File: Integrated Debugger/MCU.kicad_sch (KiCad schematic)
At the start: 14 parts, among them SW2 BOOT, U3 STM32F103CBUx, Y1 8MHz

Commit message: feat: finish routing of components
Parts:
- SW2: footprint Picoballoon Mechanical & Misc:Button GT-TC029B-H025-L1N -> Picoballoon Mechanical & Misc:Button SMD-4P,2.5x1.6mm
- Y1: footprint (none) -> Picoballoon Passives:Crystal CSTNE8M00GH5C000R0
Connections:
- net GND: now also C3.1, U3.44 (BOOT0), Y1.2
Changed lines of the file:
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@@
 	)
 	(junction
+		(at 107.95 35.56)
+		(diameter 0)
+		(color 0 0 0 0)
+	)
+	(junction
 		(at 181.61 57.15)
 		(diameter 0)
@@
 	(wire
 		(pts
+			(xy 107.95 35.56) (xy 107.95 39.37)
+		)
+		(stroke
+			(width 0)
+			(type default)
+		)
+	)
+	(wire
+		(pts
 			(xy 88.9 20.32) (xy 88.9 30.48)
 		)
@@
 	(wire
 		(pts
-			(xy 88.9 35.56) (xy 115.57 35.56)
+			(xy 88.9 35.56) (xy 107.95 35.56)
 		)
 		(stroke
@@
 	(wire
 		(pts
+			(xy 107.95 35.56) (xy 115.57 35.56)
+		)
+		(stroke
+			(width 0)
+			(type default)
+		)
+	)
+	(wire
+		(pts
 			(xy 115.57 54.61) (xy 115.57 58.42)
 		)
@@
 		)
 		(instances
-			(project ""
+			(project "Integrated Debugger"
 				(path "/ce538ebe-fda9-4af3-9f8c-9fd5bf58f0e4/b916d44a-03d1-4a04-a023-19b38caca2ea"
 					(reference "U3")
@@
 		)
 		(instances
-			(project "Programmer"
+			(project "Integrated Debugger"
 				(path "/ce538ebe-fda9-4af3-9f8c-9fd5bf58f0e4/b916d44a-03d1-4a04-a023-19b38caca2ea"
 					(reference "C7")
@@
 		)
 		(instances
-			(project "Programmer"
+			(project "Integrated Debugger"
 				(path "/ce538ebe-fda9-4af3-9f8c-9fd5bf58f0e4/b916d44a-03d1-4a04-a023-19b38caca2ea"
 					(reference "C3")
@@
 			)
 		)
-		(property "Footprint" "Picoballoon Mechanical & Misc:Button GT-TC029B-H025-L1N"
+		(property "Footprint" "Picoballoon Mechanical & Misc:Button SMD-4P,2.5x1.6mm"
 			(at 93.98 99.06 0)
 			(effects
@@
 		)
 		(instances
-			(project ""
+			(project "Integrated Debugger"
 				(path "/ce538ebe-fda9-4af3-9f8c-9fd5bf58f0e4/b916d44a-03d1-4a04-a023-19b38caca2ea"
 					(reference "SW2")
@@
 		)
 		(instances
-			(project ""
+			(project "Integrated Debugger"
 				(path "/ce538ebe-fda9-4af3-9f8c-9fd5bf58f0e4/b916d44a-03d1-4a04-a023-19b38caca2ea"
 					(reference "C4")
@@
 		)
 		(instances
-			(project "Programmer"
+			(project "Integrated Debugger"
 				(path "/ce538ebe-fda9-4af3-9f8c-9fd5bf58f0e4/b916d44a-03d1-4a04-a023-19b38caca2ea"
 					(reference "C8")
@@
 		)
 		(instances
-			(project "Programmer"
+			(project "Integrated Debugger"
 				(path "/ce538ebe-fda9-4af3-9f8c-9fd5bf58f0e4/b916d44a-03d1-4a04-a023-19b38caca2ea"
 					(reference "R14")
@@
 		)
 		(instances
-			(project "Programmer"
+			(project "Integrated Debugger"
 				(path "/ce538ebe-fda9-4af3-9f8c-9fd5bf58f0e4/b916d44a-03d1-4a04-a023-19b38caca2ea"
 					(reference "C5")
@@
 		)
 		(instances
-			(project "Programmer"
+			(project "Integrated Debugger"
 				(path "/ce538ebe-fda9-4af3-9f8c-9fd5bf58f0e4/b916d44a-03d1-4a04-a023-19b38caca2ea"
 					(reference "C6")
@@
 	(symbol
 		(lib_id "Picoballoon Power Symbols:GND")
+		(at 107.95 39.37 0)
+		(unit 1)
+		(exclude_from_sim no)
+		(in_bom yes)
+		(on_board yes)
+		(dnp no)
+		(fields_autoplaced yes)
+		(property "Reference" "#PWR019"
+			(at 107.95 45.72 0)
+			(effects
+				(font
+					(size 1.27 1.27)
+				)
+				(hide yes)
+			)
+		)
+		(property "Value" "GND"
+			(at 107.95 43.18 0)
+			(do_not_autoplace yes)
+			(effects
+				(font
+					(size 1.27 1.27)
+				)
+			)
+		)
+		(property "Footprint" ""
+			(at 107.95 39.37 0)
+			(effects
+				(font
+					(size 1.27 1.27)
+				)
+				(hide yes)
+			)
+		)
+		(property "Datasheet" ""
+			(at 107.95 39.37 0)
+			(effects
+				(font
+					(size 1.27 1.27)
+				)
+				(hide yes)
+			)
+		)
+		(property "Description" "Power symbol creates a global label with name \"GND\" , ground"
+			(at 107.95 39.37 0)
+			(effects
+				(font
+					(size 1.27 1.27)
+				)
+				(hide yes)
+			)
+		)
+		(pin "1"
+		)
+		(instances
+			(project "Integrated Debugger"
+				(path "/ce538ebe-fda9-4af3-9f8c-9fd5bf58f0e4/b916d44a-03d1-4a04-a023-19b38caca2ea"
+					(reference "#PWR019")
+					(unit 1)
+				)
+			)
+		)
+	)
+	(symbol
+		(lib_id "Picoballoon Power Symbols:GND")
 		(at 58.42 111.76 0)
 		(unit 1)
@@
 		)
 		(instances
-			(project ""
+			(project "Integrated Debugger"
 				(path "/ce538ebe-fda9-4af3-9f8c-9fd5bf58f0e4/b916d44a-03d1-4a04-a023-19b38caca2ea"
 					(reference "#PWR010")
@@
 		)
 		(instances
-			(project "Programmer"
+			(project "Integrated Debugger"
 				(path "/ce538ebe-fda9-4af3-9f8c-9fd5bf58f0e4/b916d44a-03d1-4a04-a023-19b38caca2ea"
 					(reference "R19")
@@
 		)
 		(instances
-			(project ""
+			(project "Integrated Debugger"
 				(path "/ce538ebe-fda9-4af3-9f8c-9fd5bf58f0e4/b916d44a-03d1-4a04-a023-19b38caca2ea"
 					(reference "#PWR012")
@@
 		)
 		(instances
-			(project "Programmer"
+			(project "Integrated Debugger"
 				(path "/ce538ebe-fda9-4af3-9f8c-9fd5bf58f0e4/b916d44a-03d1-4a04-a023-19b38caca2ea"
 					(reference "R15")
@@
 		)
 		(instances
-			(project "Programmer"
+			(project "Integrated Debugger"
 				(path "/ce538ebe-fda9-4af3-9f8c-9fd5bf58f0e4/b916d44a-03d1-4a04-a023-19b38caca2ea"
 					(reference "#PWR011")
@@
 		)
 		(instances
-			(project "Programmer"
+			(project "Integrated Debugger"
 				(path "/ce538ebe-fda9-4af3-9f8c-9fd5bf58f0e4/b916d44a-03d1-4a04-a023-19b38caca2ea"
 					(reference "#PWR013")
@@
 		)
 		(instances
-			(project "Programmer"
+			(project "Integrated Debugger"
 				(path "/ce538ebe-fda9-4af3-9f8c-9fd5bf58f0e4/b916d44a-03d1-4a04-a023-19b38caca2ea"
 					(reference "#PWR015")
@@
 		)
 		(instances
-			(project "Programmer"
+			(project "Integrated Debugger"
 				(path "/ce538ebe-fda9-4af3-9f8c-9fd5bf58f0e4/b916d44a-03d1-4a04-a023-19b38caca2ea"
 					(reference "C9")
@@
 		)
 		(instances
-			(project "Programmer"
+			(project "Integrated Debugger"
 				(path "/ce538ebe-fda9-4af3-9f8c-9fd5bf58f0e4/b916d44a-03d1-4a04-a023-19b38caca2ea"
 					(reference "#PWR014")
@@
 			)
 		)
-		(property "Footprint" ""
+		(property "Footprint" "Picoballoon Passives:Crystal CSTNE8M00GH5C000R0"
 			(at 78.105 40.64 0)
 			(effects
@@
 		)
 		(instances
-			(project ""
+			(project "Integrated Debugger"
 				(path "/ce538ebe-fda9-4af3-9f8c-9fd5bf58f0e4/b916d44a-03d1-4a04-a023-19b38caca2ea"
 					(reference "Y1")
@@
 		)
 		(instances
-			(project "Programmer"
+			(project "Integrated Debugger"
 				(path "/ce538ebe-fda9-4af3-9f8c-9fd5bf58f0e4/b916d44a-03d1-4a04-a023-19b38caca2ea"
 					(reference "R13")

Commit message: feat: add manufacturing data
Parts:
- C3, C4, C5, C6, C7: JLCPCB Part # (none) -> C76934; LCSC Part # (none) -> C76934; MPN (none) -> GRM033R61A104KE15D
- C8: JLCPCB Part # (none) -> C76930; LCSC Part # (none) -> C76930; MPN (none) -> GRM033R60J105MEA2D
- C9: JLCPCB Part # (none) -> C335103; LCSC Part # (none) -> C335103; MPN (none) -> GRM035R60J475ME15D
- R13, R15: JLCPCB Part # (none) -> C717002; LCSC Part # (none) -> C717002; MPN (none) -> ERJ1GNF1002C
- R14: JLCPCB Part # (none) -> C138135; LCSC Part # (none) -> C138135; MPN (none) -> RC0201FR-074K7L
- R19: JLCPCB Part # (none) -> C106227; LCSC Part # (none) -> C106227; MPN (none) -> RC0201FR-070RL
- SW2: LCSC Part # (none) -> C25168822; MPN (none) -> HX TS152605A 160gf
- U3: JLCPCB Part # (none) -> C55506; LCSC Part # (none) -> C55506; MPN (none) -> STM32F103CBU6
- Y1: JLCPCB Part # (none) -> C341525; LCSC Part # (none) -> C341525; MPN (none) -> CSTNE8M00GH5C000R0

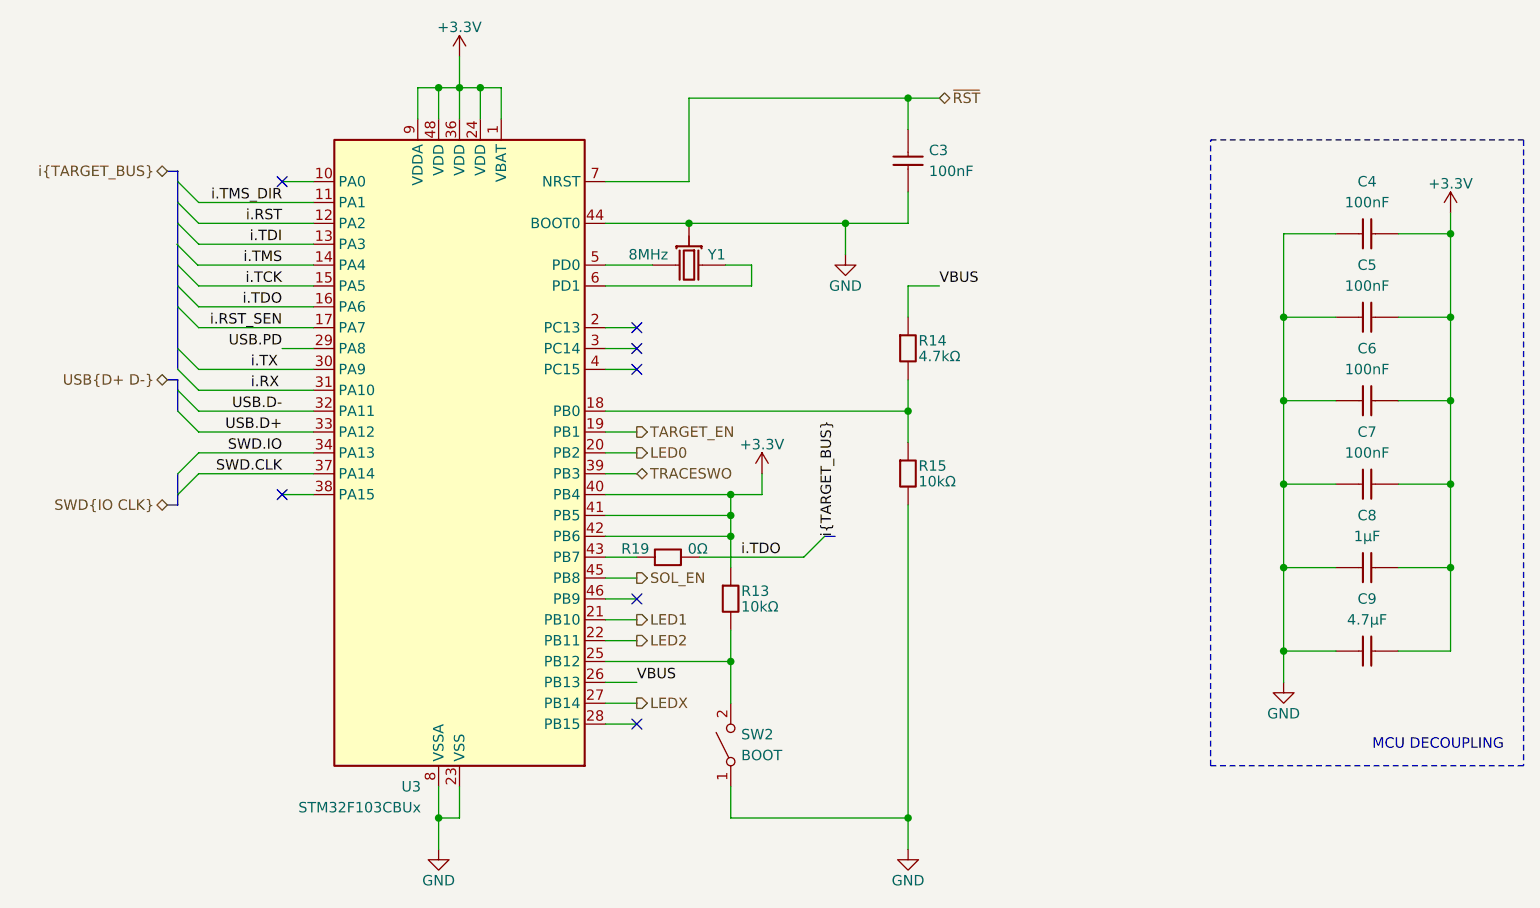
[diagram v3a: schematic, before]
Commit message: Schematic consistency improvements
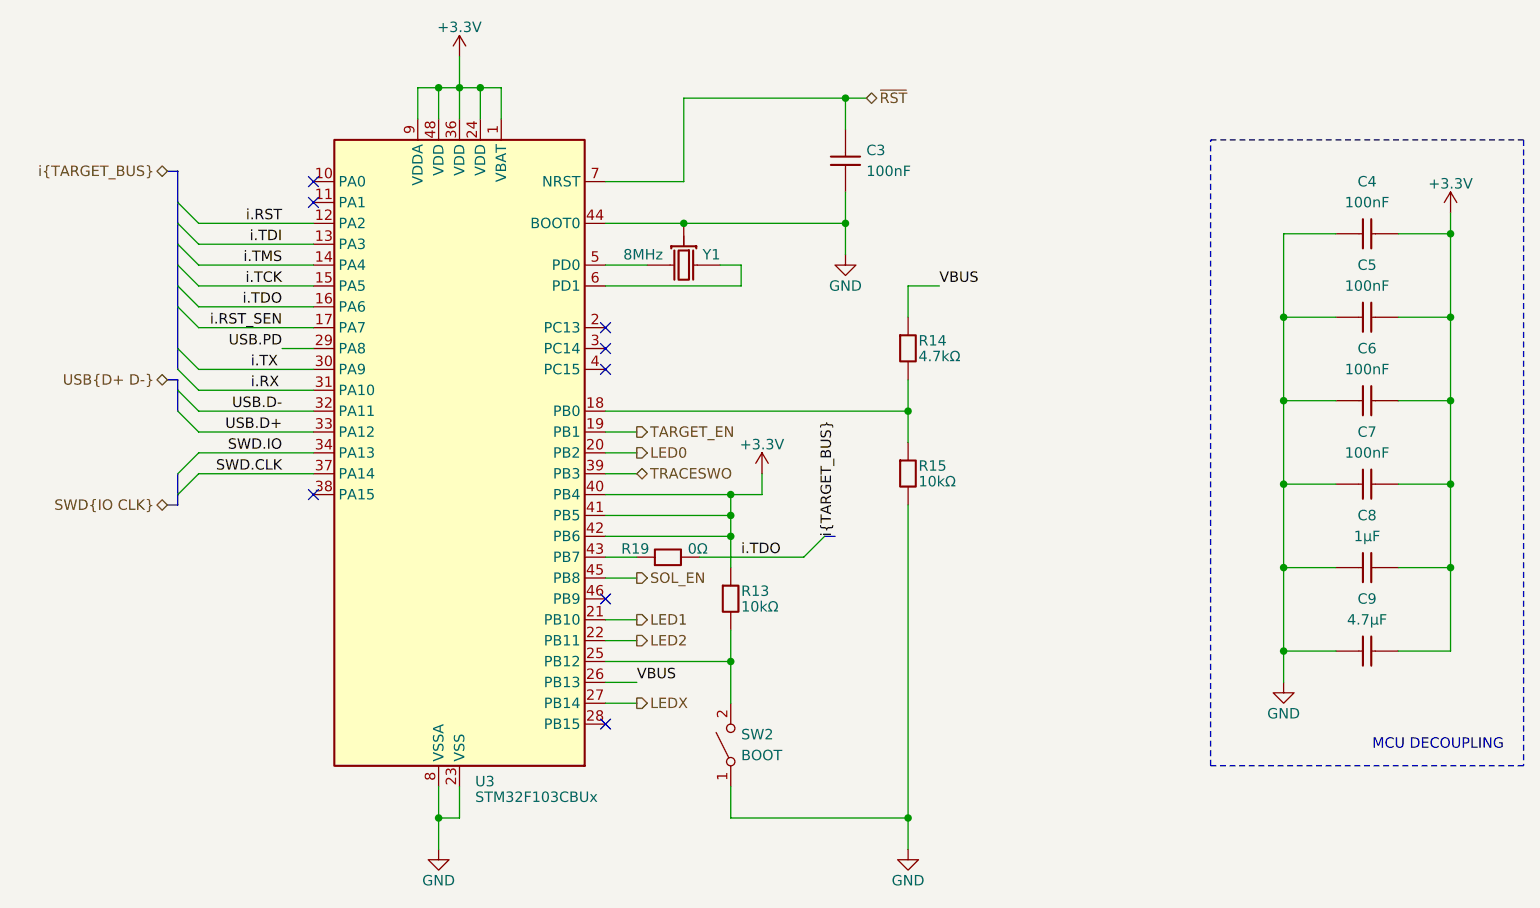
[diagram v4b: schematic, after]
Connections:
- net i.TMS_DIR: no longer names the net of U3.11 (PA1)
- no-connect marks 7 -> 8
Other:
- moved on the sheet: C3, Y1

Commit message: PCB improvements
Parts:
- renumbered C3 to C1, C4 to C2, C5 to C3, C6 to C4, C7 to C5, C8 to C6, C9 to C7, R14 to R10, R15 to R11, R19 to R8, R13 to R9, SW2 to SW1, U3 to U2
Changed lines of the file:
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@@
 	(wire
 		(pts
-			(xy 119.38 43.18) (xy 115.57 43.18)
+			(xy 121.92 43.18) (xy 115.57 43.18)
 		)
 		(stroke
@@
 	(wire
 		(pts
-			(xy 82.55 91.44) (xy 78.74 91.44)
-		)
-		(stroke
-			(width 0)
-			(type default)
-		)
-	)
-	(wire
-		(pts
 			(xy 29.21 58.42) (xy 43.18 58.42)
 		)
@@
 		)
 	)
+	(wire
+		(pts
+			(xy 78.74 91.44) (xy 88.9 91.44)
+		)
+		(stroke
+			(width 0)
+			(type default)
+		)
+	)
 	(bus
 		(pts
@@
 	)
 	(label "VBUS"
-		(at 82.55 91.44 0)
+		(at 88.9 91.44 180)
 		(effects
 			(font
 				(size 1.27 1.27)
 			)
-			(justify left bottom)
+			(justify right bottom)
 		)
 	)
@@
 	)
 	(label "VBUS"
-		(at 119.38 43.18 0)
+		(at 121.92 43.18 180)
 		(effects
 			(font
 				(size 1.27 1.27)
 			)
-			(justify left bottom)
+			(justify right bottom)
 		)
 	)
@@
 		(on_board yes)
 		(dnp no)
-		(property "Reference" "U3"
+		(property "Reference" "U2"
 			(at 62.865 103.505 0)
 			(effects
@@
 			(project "Integrated Debugger"
 				(path "/ce538ebe-fda9-4af3-9f8c-9fd5bf58f0e4/b916d44a-03d1-4a04-a023-19b38caca2ea"
-					(reference "U3")
+					(reference "U2")
 					(unit 1)
 				)
@@
 		(dnp no)
 		(fields_autoplaced yes)
-		(property "Reference" "C7"
+		(property "Reference" "C5"
 			(at 171.45 60.96 90)
 			(effects
@@
 			(project "Integrated Debugger"
 				(path "/ce538ebe-fda9-4af3-9f8c-9fd5bf58f0e4/b916d44a-03d1-4a04-a023-19b38caca2ea"
-					(reference "C7")
+					(reference "C5")
 					(unit 1)
 				)
@@
 		(dnp no)
 		(fields_autoplaced yes)
-		(property "Reference" "C3"
+		(property "Reference" "C1"
 			(at 110.49 26.6699 0)
 			(effects
@@
 			(project "Integrated Debugger"
 				(path "/ce538ebe-fda9-4af3-9f8c-9fd5bf58f0e4/b916d44a-03d1-4a04-a023-19b38caca2ea"
-					(reference "C3")
+					(reference "C1")
 					(unit 1)
 				)
@@
 		(dnp no)
 		(fields_autoplaced yes)
-		(property "Reference" "SW2"
+		(property "Reference" "SW1"
 			(at 95.25 97.7899 90)
 			(effects
@@
 			(project "Integrated Debugger"
 				(path "/ce538ebe-fda9-4af3-9f8c-9fd5bf58f0e4/b916d44a-03d1-4a04-a023-19b38caca2ea"
-					(reference "SW2")
+					(reference "SW1")
 					(unit 1)
 				)
@@
 		(dnp no)
 		(fields_autoplaced yes)
-		(property "Reference" "C4"
+		(property "Reference" "C2"
 			(at 171.45 30.48 90)
 			(effects
@@
 			(project "Integrated Debugger"
 				(path "/ce538ebe-fda9-4af3-9f8c-9fd5bf58f0e4/b916d44a-03d1-4a04-a023-19b38caca2ea"
-					(reference "C4")
+					(reference "C2")
 					(unit 1)
 				)
@@
 		(dnp no)
 		(fields_autoplaced yes)
-		(property "Reference" "C8"
+		(property "Reference" "C6"
 			(at 171.45 71.12 90)
 			(effects
@@
 			(project "Integrated Debugger"
 				(path "/ce538ebe-fda9-4af3-9f8c-9fd5bf58f0e4/b916d44a-03d1-4a04-a023-19b38caca2ea"
-					(reference "C8")
+					(reference "C6")
 					(unit 1)
 				)
@@
 		(dnp no)
 		(fields_autoplaced yes)
-		(property "Reference" "R14"
+		(property "Reference" "R10"
 			(at 116.84 49.8475 0)
 			(do_not_autoplace yes)
@@
 			(project "Integrated Debugger"
 				(path "/ce538ebe-fda9-4af3-9f8c-9fd5bf58f0e4/b916d44a-03d1-4a04-a023-19b38caca2ea"
-					(reference "R14")
+					(reference "R10")
 					(unit 1)
 				)
@@
 		(dnp no)
 		(fields_autoplaced yes)
-		(property "Reference" "C5"
+		(property "Reference" "C3"
 			(at 171.45 40.64 90)
 			(effects
@@
 			(project "Integrated Debugger"
 				(path "/ce538ebe-fda9-4af3-9f8c-9fd5bf58f0e4/b916d44a-03d1-4a04-a023-19b38caca2ea"
-					(reference "C5")
+					(reference "C3")
 					(unit 1)
 				)
@@
 		(dnp no)
 		(fields_autoplaced yes)
-		(property "Reference" "C6"
+		(property "Reference" "C4"
 			(at 171.45 50.8 90)
 			(effects
@@
 			(project "Integrated Debugger"
 				(path "/ce538ebe-fda9-4af3-9f8c-9fd5bf58f0e4/b916d44a-03d1-4a04-a023-19b38caca2ea"
-					(reference "C6")
+					(reference "C4")
 					(unit 1)
 				)
@@
 		(dnp no)
 		(fields_autoplaced yes)
-		(property "Reference" "#PWR019"
+		(property "Reference" "#PWR010"
 			(at 107.95 45.72 0)
 			(effects
@@
 			(project "Integrated Debugger"
 				(path "/ce538ebe-fda9-4af3-9f8c-9fd5bf58f0e4/b916d44a-03d1-4a04-a023-19b38caca2ea"
-					(reference "#PWR019")
+					(reference "#PWR010")
 					(unit 1)
 				)
@@
 		(dnp no)
 		(fields_autoplaced yes)
-		(property "Reference" "#PWR010"
+		(property "Reference" "#PWR07"
 			(at 58.42 118.11 0)
 			(effects
@@
 			(project "Integrated Debugger"
 				(path "/ce538ebe-fda9-4af3-9f8c-9fd5bf58f0e4/b916d44a-03d1-4a04-a023-19b38caca2ea"
-					(reference "#PWR010")
+					(reference "#PWR07")
 					(unit 1)
 				)
@@
 		(on_board yes)
 		(dnp no)
-		(property "Reference" "R19"
+		(property "Reference" "R8"
 			(at 84.074 75.184 90)
 			(do_not_autoplace yes)
@@
 			(project "Integrated Debugger"
 				(path "/ce538ebe-fda9-4af3-9f8c-9fd5bf58f0e4/b916d44a-03d1-4a04-a023-19b38caca2ea"
-					(reference "R19")
+					(reference "R8")
 					(unit 1)
 				)
@@
 		(dnp no)
 		(fields_autoplaced yes)
-		(property "Reference" "#PWR012"
+		(property "Reference" "#PWR09"
 			(at 97.79 69.85 0)
 			(effects
@@
 			(project "Integrated Debugger"
 				(path "/ce538ebe-fda9-4af3-9f8c-9fd5bf58f0e4/b916d44a-03d1-4a04-a023-19b38caca2ea"
-					(reference "#PWR012")
+					(reference "#PWR09")
 					(unit 1)
 				)
@@
 		(dnp no)
 		(fields_autoplaced yes)
-		(property "Reference" "R15"
+		(property "Reference" "R11"
 			(at 116.84 65.0875 0)
 			(do_not_autoplace yes)
@@
 			(project "Integrated Debugger"
 				(path "/ce538ebe-fda9-4af3-9f8c-9fd5bf58f0e4/b916d44a-03d1-4a04-a023-19b38caca2ea"
-					(reference "R15")
+					(reference "R11")
 					(unit 1)
 				)
@@
 		(dnp no)
 		(fields_autoplaced yes)
-		(property "Reference" "#PWR011"
+		(property "Reference" "#PWR08"
 			(at 60.96 19.05 0)
 			(effects
@@
 			(project "Integrated Debugger"
 				(path "/ce538ebe-fda9-4af3-9f8c-9fd5bf58f0e4/b916d44a-03d1-4a04-a023-19b38caca2ea"
-					(reference "#PWR011")
+					(reference "#PWR08")
 					(unit 1)
 				)
@@
 		(dnp no)
 		(fields_autoplaced yes)
-		(property "Reference" "#PWR013"
+		(property "Reference" "#PWR011"
 			(at 115.57 118.11 0)
 			(effects
@@
 			(project "Integrated Debugger"
 				(path "/ce538ebe-fda9-4af3-9f8c-9fd5bf58f0e4/b916d44a-03d1-4a04-a023-19b38caca2ea"
-					(reference "#PWR013")
+					(reference "#PWR011")
 					(unit 1)
 				)
@@
 		(dnp no)
 		(fields_autoplaced yes)
-		(property "Reference" "#PWR015"
+		(property "Reference" "#PWR013"
 			(at 181.61 38.1 0)
 			(effects
@@
 			(project "Integrated Debugger"
 				(path "/ce538ebe-fda9-4af3-9f8c-9fd5bf58f0e4/b916d44a-03d1-4a04-a023-19b38caca2ea"
-					(reference "#PWR015")
+					(reference "#PWR013")
 					(unit 1)
 				)
@@
 		(dnp no)
 		(fields_autoplaced yes)
-		(property "Reference" "C9"
+		(property "Reference" "C7"
 			(at 171.45 81.28 90)
 			(effects
@@
 			(project "Integrated Debugger"
 				(path "/ce538ebe-fda9-4af3-9f8c-9fd5bf58f0e4/b916d44a-03d1-4a04-a023-19b38caca2ea"
-					(reference "C9")
+					(reference "C7")
 					(unit 1)
 				)
@@
 		(dnp no)
 		(fields_autoplaced yes)
-		(property "Reference" "#PWR014"
+		(property "Reference" "#PWR012"
 			(at 161.29 97.79 0)
 			(effects
@@
 			(project "Integrated Debugger"
 				(path "/ce538ebe-fda9-4af3-9f8c-9fd5bf58f0e4/b916d44a-03d1-4a04-a023-19b38caca2ea"
-					(reference "#PWR014")
+					(reference "#PWR012")
 					(unit 1)
 				)
@@
 		(dnp no)
 		(fields_autoplaced yes)
-		(property "Reference" "R13"
+		(property "Reference" "R9"
 			(at 95.25 80.3275 0)
 			(do_not_autoplace yes)
@@
 			(project "Integrated Debugger"
 				(path "/ce538ebe-fda9-4af3-9f8c-9fd5bf58f0e4/b916d44a-03d1-4a04-a023-19b38caca2ea"
-					(reference "R13")
+					(reference "R9")
 					(unit 1)
 				)

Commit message: feat: debugger flip swd connector, usb patch + stackup change
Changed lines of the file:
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@@
-		)
-	)
-	(label "USB.PD"
-		(at 39.37 50.8 180)
-		(effects
-			(font
-				(size 1.27 1.27)
-			)
-			(justify right bottom)
 		)
 	)
@@
 		)
 	)
+	(hierarchical_label "USB.PD"
+		(shape passive)
+		(at 39.37 50.8 180)
+		(effects
+			(font
+				(size 1.27 1.27)
+			)
+			(justify right)
+		)
+	)
